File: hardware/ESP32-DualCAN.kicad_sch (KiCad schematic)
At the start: 31 parts, among them J1 Molex 70553 6p, J2 Conn_01x10_Socket, J3 Conn_01x10_Socket, J4 holes, J5 pads, J6 holes, J7 pads, U1 LV2862Y, U2 ESP32-C6-SuperMini, U3 TCAN1044AV, U4 TCAN1044AV, U5 ESP32-C6-Zero

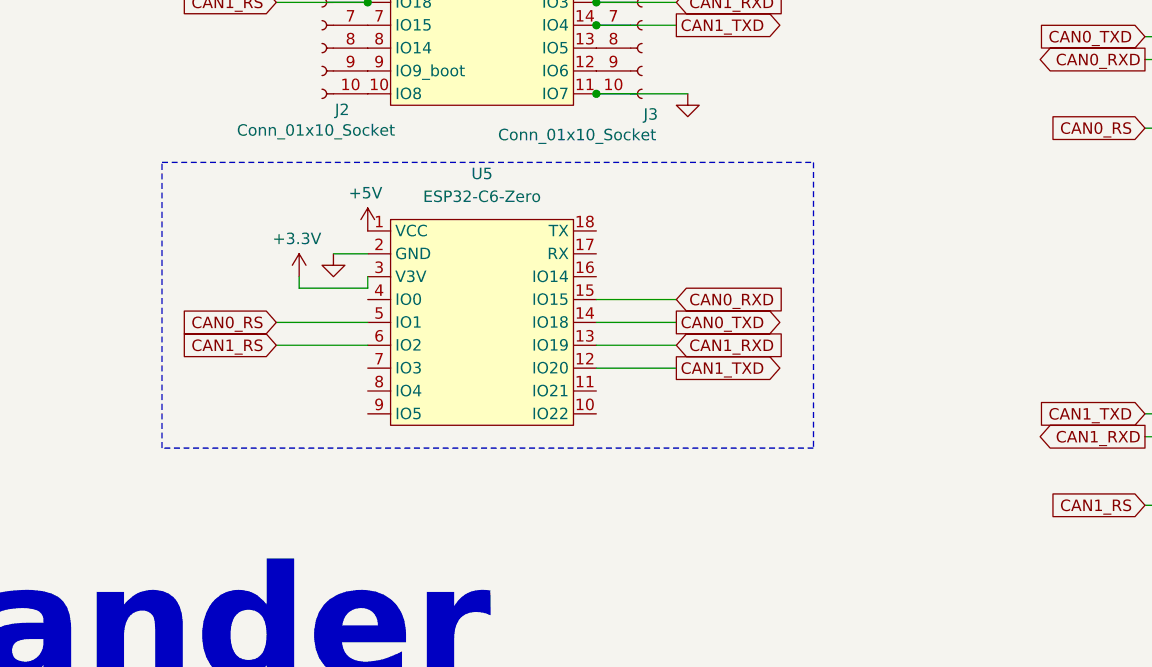
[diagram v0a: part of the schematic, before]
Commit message: ESP32-C6-Zero alternative comments
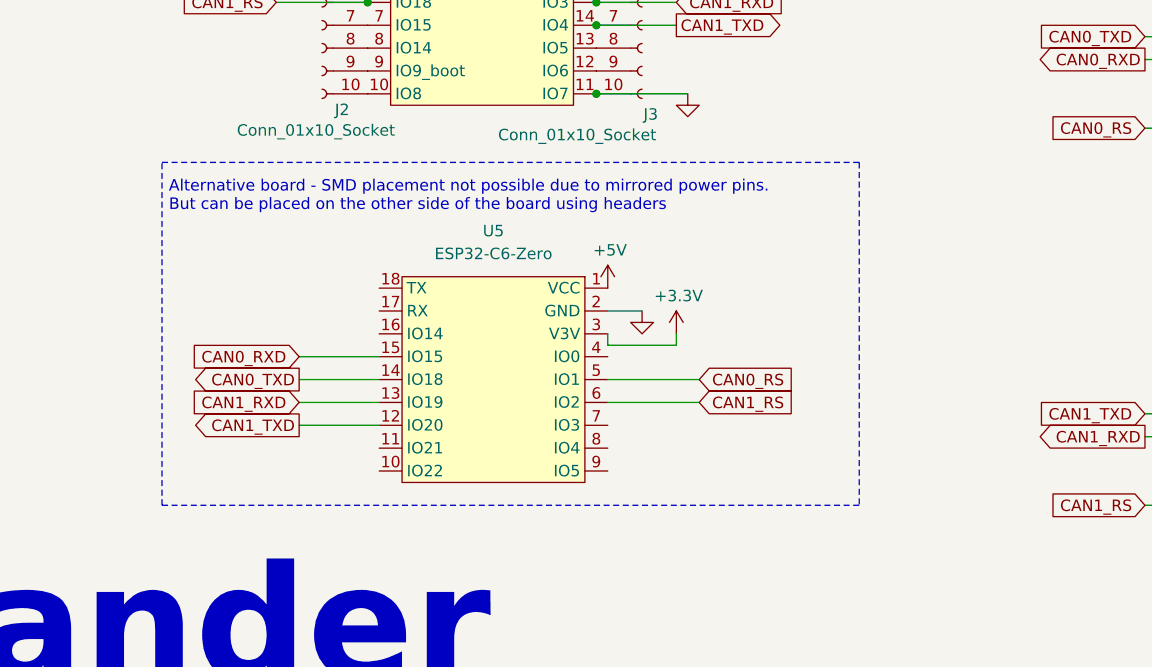
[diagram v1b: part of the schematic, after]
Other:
- note added: "Alternative board - SMD placement not possible due to mirrored power pins. But can be placed on the other side of the board using headers"
- moved on the sheet: U5
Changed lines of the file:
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@@
 	(rectangle
 		(start 100.33 107.95)
-		(end 172.72 139.7)
+		(end 177.8 146.05)
 		(stroke
 			(width 0)
@@
 		)
 	)
+	(text "Alternative board - SMD placement not possible due to mirrored power pins.\nBut can be placed on the other side of the board using headers"
+		(exclude_from_sim no)
+		(at 101.092 111.76 0)
+		(effects
+			(font
+				(size 1.27 1.27)
+			)
+			(justify left)
+		)
+	)
 	(text "Dorky\nCommander"
 		(exclude_from_sim no)
@@
 	(wire
 		(pts
-			(xy 157.48 125.73) (xy 148.59 125.73)
+			(xy 115.57 132.08) (xy 124.46 132.08)
 		)
 		(stroke
@@
 	(wire
 		(pts
-			(xy 115.57 121.92) (xy 123.19 121.92)
+			(xy 157.48 128.27) (xy 149.86 128.27)
 		)
 		(stroke
@@
 	(wire
 		(pts
-			(xy 113.03 125.73) (xy 123.19 125.73)
+			(xy 160.02 132.08) (xy 149.86 132.08)
 		)
 		(stroke
@@
 	(wire
 		(pts
-			(xy 123.19 121.92) (xy 123.19 120.65)
+			(xy 149.86 128.27) (xy 149.86 127)
 		)
 		(stroke
@@
 	(wire
 		(pts
-			(xy 157.48 130.81) (xy 148.59 130.81)
+			(xy 115.57 137.16) (xy 124.46 137.16)
 		)
 		(stroke
@@
 	(wire
 		(pts
-			(xy 157.48 123.19) (xy 148.59 123.19)
+			(xy 115.57 129.54) (xy 124.46 129.54)
 		)
 		(stroke
@@
 	(wire
 		(pts
-			(xy 119.38 118.11) (xy 123.19 118.11)
+			(xy 153.67 124.46) (xy 149.86 124.46)
 		)
 		(stroke
@@
 	(wire
 		(pts
-			(xy 157.48 128.27) (xy 148.59 128.27)
+			(xy 115.57 134.62) (xy 124.46 134.62)
 		)
 		(stroke
@@
 	(wire
 		(pts
-			(xy 115.57 121.92) (xy 115.57 120.65)
+			(xy 157.48 128.27) (xy 157.48 127)
 		)
 		(stroke
@@
 	(wire
 		(pts
-			(xy 113.03 128.27) (xy 123.19 128.27)
+			(xy 160.02 134.62) (xy 149.86 134.62)
 		)
 		(stroke
@@
 	(global_label "CAN0_TXD"
 		(shape output)
-		(at 157.48 125.73 0)
+		(at 115.57 132.08 180)
 		(fields_autoplaced yes)
 		(effects
@@
 				(size 1.27 1.27)
 			)
-			(justify left)
+			(justify right)
 		)
 		(property "Intersheetrefs" "${INTERSHEET_REFS}"
-			(at 169.7785 125.73 0)
+			(at 103.2715 132.08 0)
 			(hide yes)
 			(show_name no)
@@
 					(size 1.27 1.27)
 				)
-				(justify left)
+				(justify right)
 			)
 		)
@@
 	(global_label "CAN1_RXD"
 		(shape input)
-		(at 157.48 128.27 0)
+		(at 115.57 134.62 180)
 		(fields_autoplaced yes)
 		(effects
@@
 				(size 1.27 1.27)
 			)
-			(justify left)
+			(justify right)
 		)
 		(property "Intersheetrefs" "${INTERSHEET_REFS}"
-			(at 170.0809 128.27 0)
+			(at 102.9691 134.62 0)
 			(hide yes)
 			(show_name no)
@@
 					(size 1.27 1.27)
 				)
-				(justify left)
+				(justify right)
 			)
 		)
@@
 	(global_label "CAN1_RS"
 		(shape input)
-		(at 113.03 128.27 180)
+		(at 160.02 134.62 0)
 		(fields_autoplaced yes)
 		(effects
@@
 				(size 1.27 1.27)
 			)
-			(justify right)
+			(justify left)
 		)
 		(property "Intersheetrefs" "${INTERSHEET_REFS}"
-			(at 101.6991 128.27 0)
+			(at 171.3509 134.62 0)
 			(hide yes)
 			(show_name no)
@@
 					(size 1.27 1.27)
 				)
-				(justify right)
+				(justify left)
 			)
 		)
@@
 	(global_label "CAN0_RXD"
 		(shape input)
-		(at 157.48 123.19 0)
+		(at 115.57 129.54 180)
 		(fields_autoplaced yes)
 		(effects
@@
 				(size 1.27 1.27)
 			)
-			(justify left)
+			(justify right)
 		)
 		(property "Intersheetrefs" "${INTERSHEET_REFS}"
-			(at 170.0809 123.19 0)
+			(at 102.9691 129.54 0)
 			(hide yes)
 			(show_name no)
@@
 					(size 1.27 1.27)
 				)
-				(justify left)
+				(justify right)
 			)
 		)
@@
 	(global_label "CAN0_RS"
 		(shape input)
-		(at 113.03 125.73 180)
+		(at 160.02 132.08 0)
 		(fields_autoplaced yes)
 		(effects
@@
 				(size 1.27 1.27)
 			)
-			(justify right)
+			(justify left)
 		)
 		(property "Intersheetrefs" "${INTERSHEET_REFS}"
-			(at 101.6991 125.73 0)
+			(at 171.3509 132.08 0)
 			(hide yes)
 			(show_name no)
@@
 					(size 1.27 1.27)
 				)
-				(justify right)
+				(justify left)
 			)
 		)
@@
 	(global_label "CAN1_TXD"
 		(shape output)
-		(at 157.48 130.81 0)
+		(at 115.57 137.16 180)
 		(fields_autoplaced yes)
 		(effects
@@
 				(size 1.27 1.27)
 			)
-			(justify left)
+			(justify right)
 		)
 		(property "Intersheetrefs" "${INTERSHEET_REFS}"
-			(at 169.7785 130.81 0)
+			(at 103.2715 137.16 0)
 			(hide yes)
 			(show_name no)
@@
 					(size 1.27 1.27)
 				)
-				(justify left)
+				(justify right)
 			)
 		)
@@
 	(symbol
 		(lib_id "power:+3.3V")
-		(at 123.19 115.57 0)
+		(at 149.86 121.92 0)
+		(mirror y)
 		(unit 1)
 		(body_style 1)
@@
 		(dnp no)
 		(property "Reference" "#PWR016"
-			(at 123.19 119.38 0)
+			(at 149.86 125.73 0)
 			(hide yes)
 			(show_name no)
@@
 		)
 		(property "Value" "+5V"
-			(at 122.9419 111.3621 0)
+			(at 150.1081 117.7121 0)
 			(show_name no)
 			(do_not_autoplace no)
@@
 		)
 		(property "Footprint" ""
-			(at 123.19 115.57 0)
+			(at 149.86 121.92 0)
 			(hide yes)
 			(show_name no)
@@
 		)
 		(property "Datasheet" ""
-			(at 123.19 115.57 0)
+			(at 149.86 121.92 0)
 			(hide yes)
 			(show_name no)
@@
 		)
 		(property "Description" "Power symbol creates a global label with name \"+3.3V\""
-			(at 123.19 115.57 0)
+			(at 149.86 121.92 0)
 			(hide yes)
 			(show_name no)
@@
 	(symbol
 		(lib_id "esp:Waveshare-ESP32-C6-Zero")
-		(at 135.89 125.73 0)
+		(at 137.16 132.08 0)
+		(mirror y)
 		(unit 1)
 		(body_style 1)
@@
 		(dnp no)
 		(property "Reference" "U5"
-			(at 135.89 109.22 0)
+			(at 137.16 115.57 0)
 			(show_name no)
 			(do_not_autoplace no)
@@
 		)
 		(property "Value" "ESP32-C6-Zero"
-			(at 135.89 111.76 0)
+			(at 137.16 118.11 0)
 			(show_name no)
 			(do_not_autoplace no)
@@
 		)
 		(property "Footprint" "Waveshare-ESP32:Waveshare-ESP32-C6-Zero"
-			(at 135.89 139.446 0)
+			(at 137.16 145.796 0)
 			(hide yes)
 			(show_name no)
@@
 		)
 		(property "Datasheet" "https://www.waveshare.com/wiki/ESP32-C6-Zero"
-			(at 135.636 141.986 0)
+			(at 137.414 148.336 0)
 			(hide yes)
 			(show_name no)
@@
 		)
 		(property "Description" ""
-			(at 125.73 115.57 0)
+			(at 147.32 121.92 0)
 			(hide yes)
 			(show_name no)
@@
 	(symbol
 		(lib_id "power:+3.3V")
-		(at 115.57 120.65 0)
+		(at 157.48 127 0)
+		(mirror y)
 		(unit 1)
 		(body_style 1)
@@
 		(dnp no)
 		(property "Reference" "#PWR018"
-			(at 115.57 124.46 0)
+			(at 157.48 130.81 0)
 			(hide yes)
 			(show_name no)
@@
 		)
 		(property "Value" "+3.3V"
-			(at 115.3219 116.4421 0)
+			(at 157.7281 122.7921 0)
 			(show_name no)
 			(do_not_autoplace no)
@@
 		)
 		(property "Footprint" ""
-			(at 115.57 120.65 0)
+			(at 157.48 127 0)
 			(hide yes)
 			(show_name no)
@@
 		)
 		(property "Datasheet" ""
-			(at 115.57 120.65 0)
+			(at 157.48 127 0)
 			(hide yes)
 			(show_name no)
@@
 		)
 		(property "Description" "Power symbol creates a global label with name \"+3.3V\""
-			(at 115.57 120.65 0)
+			(at 157.48 127 0)
 			(hide yes)
 			(show_name no)
@@
 	(symbol
 		(lib_id "power:GND")
-		(at 119.38 118.11 0)
+		(at 153.67 124.46 0)
+		(mirror y)
 		(unit 1)
 		(body_style 1)
@@
 		(dnp no)
 		(property "Reference" "#PWR019"
-			(at 119.38 124.46 0)
+			(at 153.67 130.81 0)
 			(hide yes)
 			(show_name no)
@@
 		)
 		(property "Value" "GND"
-			(at 120.65 120.65 0)
+			(at 152.4 127 0)
 			(hide yes)
 			(show_name no)
@@
 		)
 		(property "Footprint" ""
-			(at 119.38 118.11 0)
+			(at 153.67 124.46 0)
 			(hide yes)
 			(show_name no)
@@
 		)
 		(property "Datasheet" ""
-			(at 119.38 118.11 0)
+			(at 153.67 124.46 0)
 			(hide yes)
 			(show_name no)
@@
 		)
 		(property "Description" ""
-			(at 119.38 118.11 0)
+			(at 153.67 124.46 0)
 			(hide yes)
 			(show_name no)

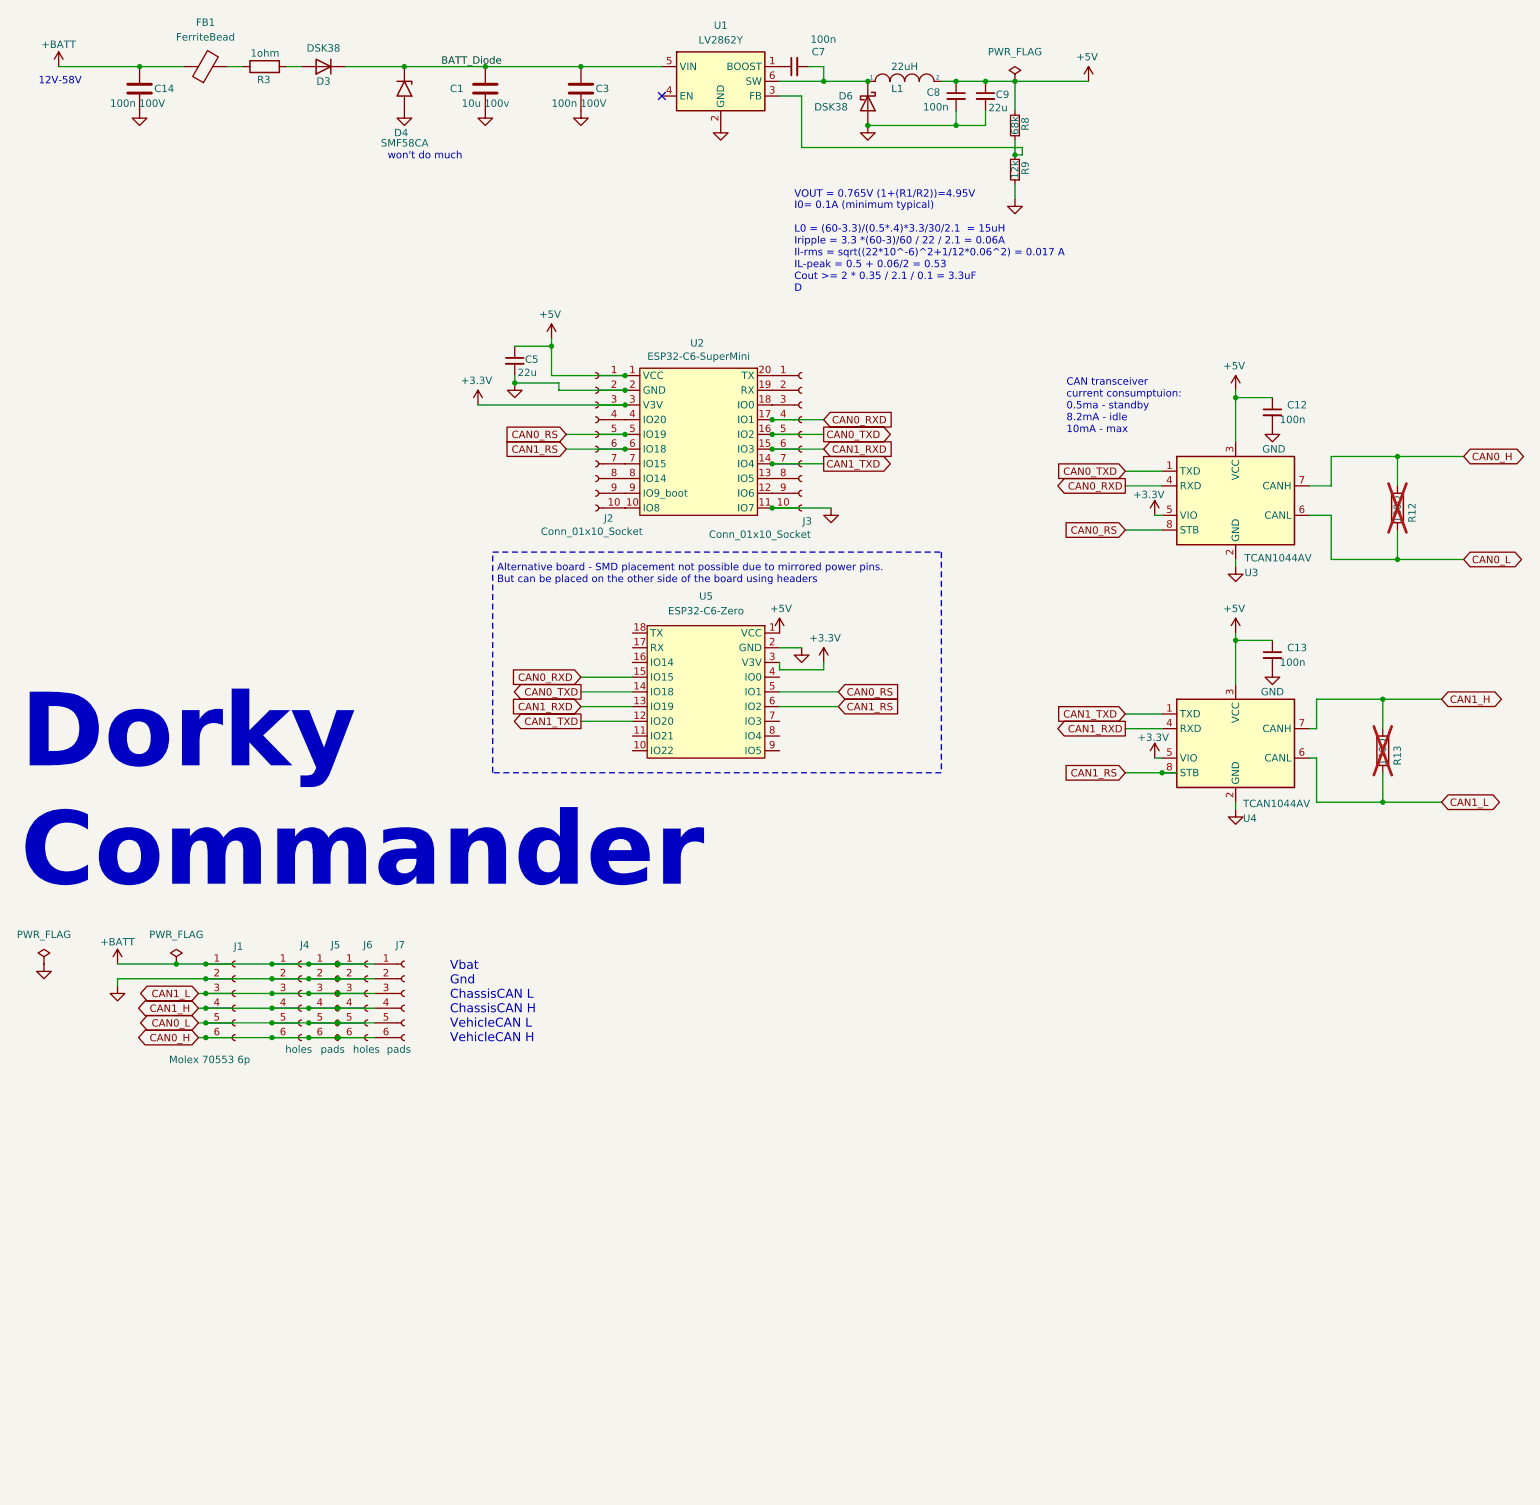
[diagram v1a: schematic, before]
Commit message: Use 8MB ESP32-C6-Zero
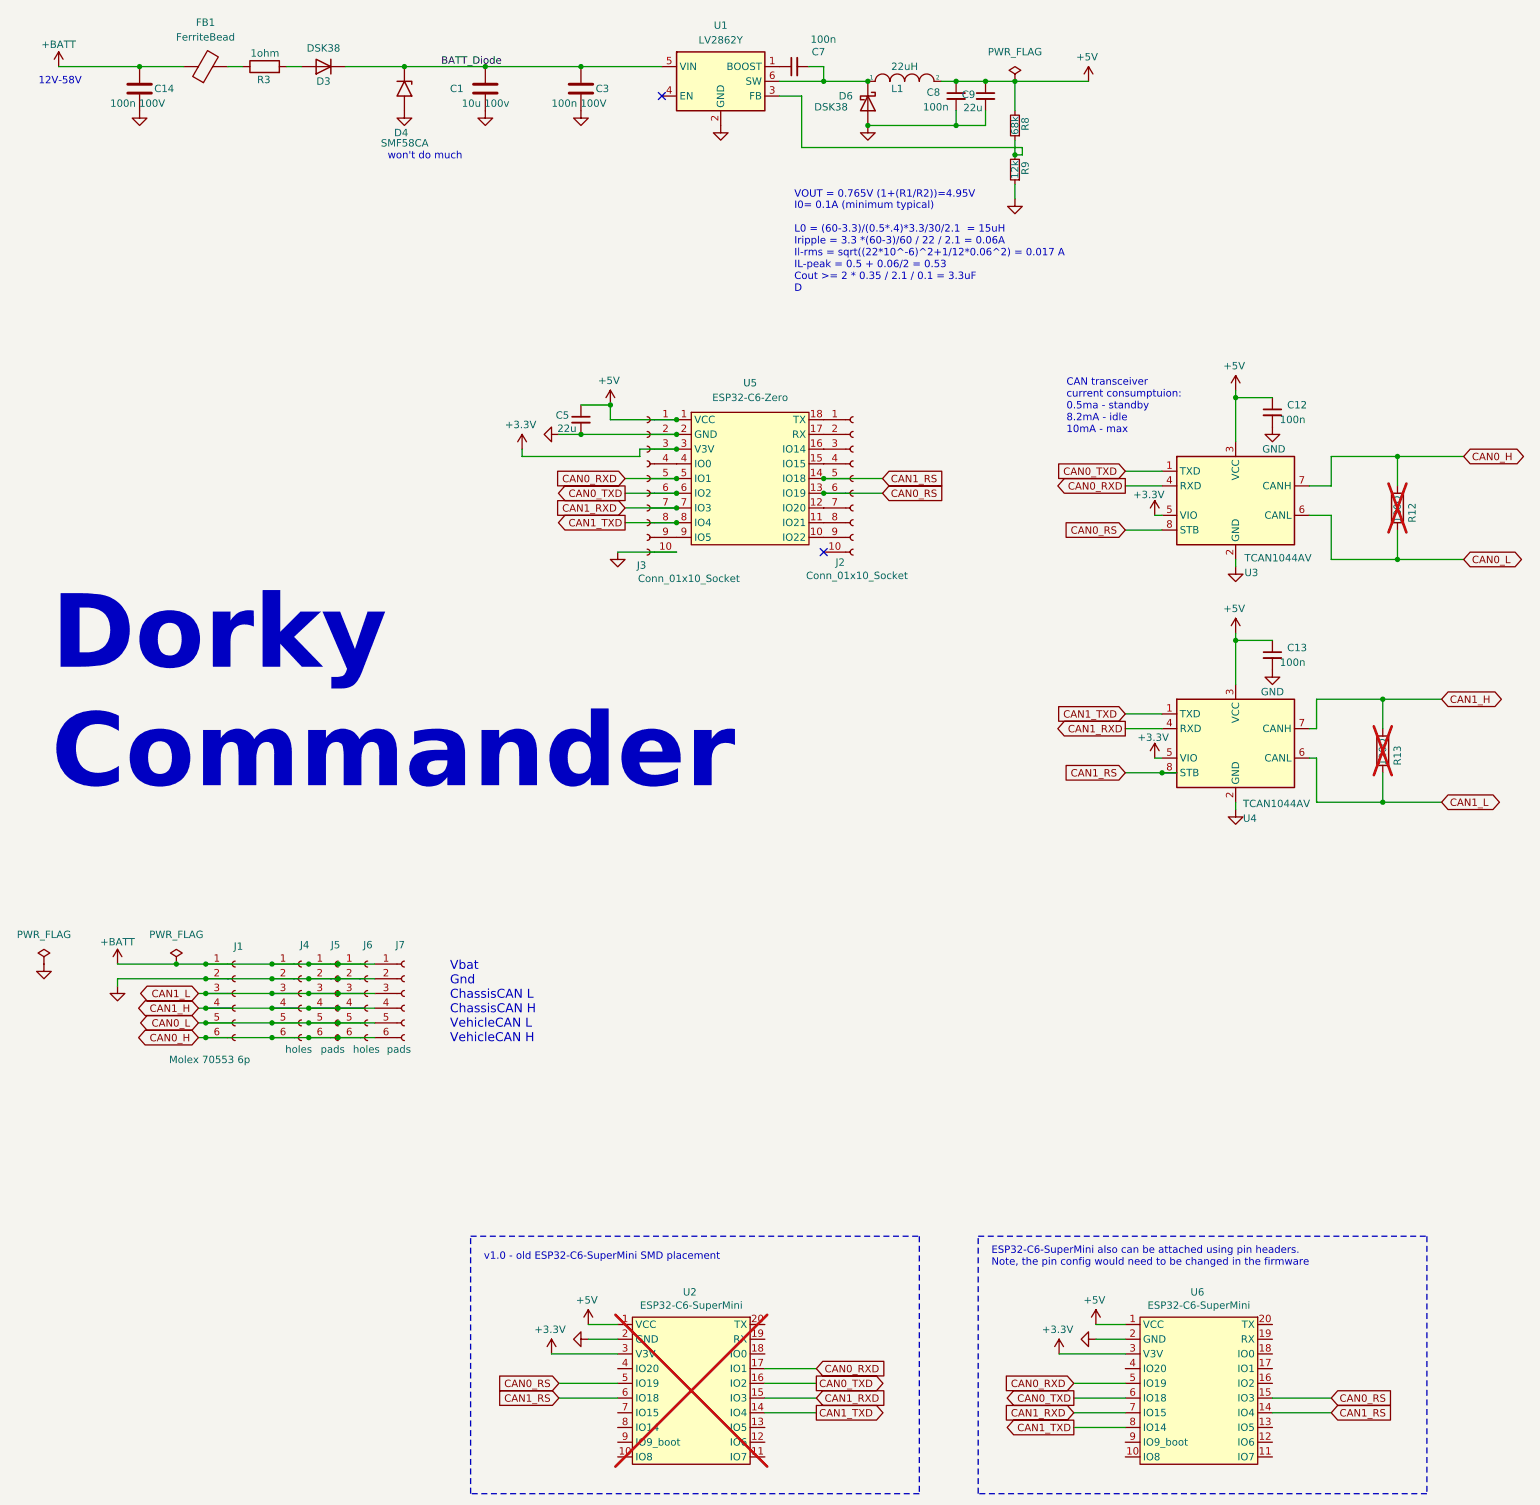
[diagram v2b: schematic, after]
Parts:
- added U6: ESP32-C6-SuperMini, lib:ESP32-C6-SuperMini, symbol esp:ESP32-C6-SuperMini
- U2: now not fitted
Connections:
- net +3.3V: now also J3.3 (Pin_3), U6.3 (V3V); no longer J2.3 (Pin_3)
- net +5V: now also J3.1 (Pin_1), U6.1 (VCC); no longer J2.1 (Pin_1)
- net CAN0_RS: now also J2.6 (Pin_6), U5.13 (IO19), U6.15 (IO3); no longer J2.5 (Pin_5), U5.5 (IO1)
- net CAN0_RXD: now also J3.5 (Pin_5), U5.5 (IO1), U6.5 (IO19); no longer J3.4 (Pin_4), U5.15 (IO15)
- net CAN0_TXD: now also J3.6 (Pin_6), U5.6 (IO2), U6.6 (IO18); no longer J3.5 (Pin_5), U5.14 (IO18)
- net CAN1_RS: now also J2.5 (Pin_5), U5.14 (IO18), U6.14 (IO4); no longer J2.6 (Pin_6), U5.6 (IO2)
- net CAN1_RXD: now also J3.7 (Pin_7), U5.7 (IO3), U6.7 (IO15); no longer J3.6 (Pin_6), U5.13 (IO19)
- net CAN1_TXD: now also J3.8 (Pin_8), U5.8 (IO4), U6.8 (IO14); no longer J3.7 (Pin_7), U5.12 (IO20)
- net GND: now also J3.2 (Pin_2), U6.2 (GND); no longer J2.2 (Pin_2), U2.11 (IO7)
- net at J2.10 (Pin_10): no longer U2.10 (IO8)
- net at J2.4 (Pin_4): now also U5.15 (IO15); no longer U2.4 (IO20)
- net at J2.7 (Pin_7): now also U5.12 (IO20); no longer U2.7 (IO15)
- net at J2.8 (Pin_8): now also U5.11 (IO21); no longer U2.8 (IO14)
- net at J2.9 (Pin_9): now also U5.10 (IO22); no longer U2.9 (IO9_boot)
- net at U2.12 (IO6): no longer J3.9 (Pin_9)
- net at U2.13 (IO5): no longer J3.8 (Pin_8)
- net at U2.18 (IO0): no longer J3.3 (Pin_3)
- net at U2.19 (RX): no longer J3.2 (Pin_2)
- net at U2.20 (TX): no longer J3.1 (Pin_1)
- net at U5.16 (IO14): now also J2.3 (Pin_3)
- net at U5.17 (RX): now also J2.2 (Pin_2)
- net at U5.18 (TX): now also J2.1 (Pin_1)
- net at U5.4 (IO0): now also J3.4 (Pin_4)
- net at U5.9 (IO5): now also J3.9 (Pin_9)
- no-connect marks 1 -> 2
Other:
- note added: "ESP32-C6-SuperMini also can be attached using pin headers. Note, the pin config would need to be changed in the firmware"
- note added: "v1.0 - old ESP32-C6-SuperMini SMD placement"
- note removed: "Alternative board - SMD placement not possible due to mirrored power pins. But can be placed on the other side of the board using headers"
- moved on the sheet: C5, J2, J3, U5

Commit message: cheap connector
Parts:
- J1: LCSC C505298 -> C24361
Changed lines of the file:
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@@
 			)
 		)
-		(property "LCSC" "C505298"
+		(property "LCSC" "C24361"
 			(at 55.88 184.15 0)
 			(hide yes)
